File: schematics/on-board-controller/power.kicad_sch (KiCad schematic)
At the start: 20 parts, among them J3 xt60, U6 L78L33_TO92, U7 L7806

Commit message: changed size of electrolytic capacitors
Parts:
- C4, C5, C6: footprint Capacitor_THT:CP_Radial_D14.0mm_P7.50mm -> Capacitor_THT:CP_Radial_D12.5mm_P5.00mm
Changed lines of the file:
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@@
 			)
 		)
-		(property "Footprint" "Capacitor_THT:CP_Radial_D14.0mm_P7.50mm"
+		(property "Footprint" "Capacitor_THT:CP_Radial_D12.5mm_P5.00mm"
 			(at 144.4752 100.33 0)
 			(effects
@@
 			)
 		)
-		(property "Footprint" "Capacitor_THT:CP_Radial_D14.0mm_P7.50mm"
+		(property "Footprint" "Capacitor_THT:CP_Radial_D12.5mm_P5.00mm"
 			(at 67.0052 77.47 0)
 			(effects
@@
 			)
 		)
-		(property "Footprint" "Capacitor_THT:CP_Radial_D14.0mm_P7.50mm"
+		(property "Footprint" "Capacitor_THT:CP_Radial_D12.5mm_P5.00mm"
 			(at 87.63 45.4152 0)
 			(effects

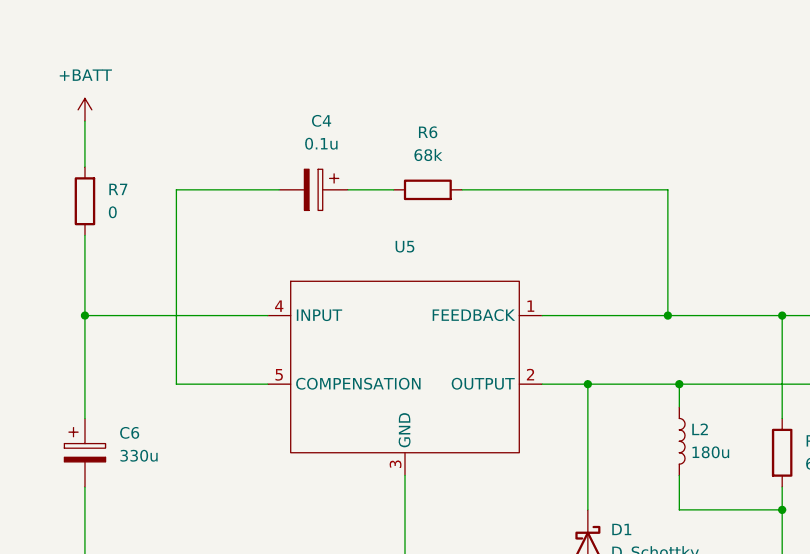
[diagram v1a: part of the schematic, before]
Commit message: updated names of components on schematic
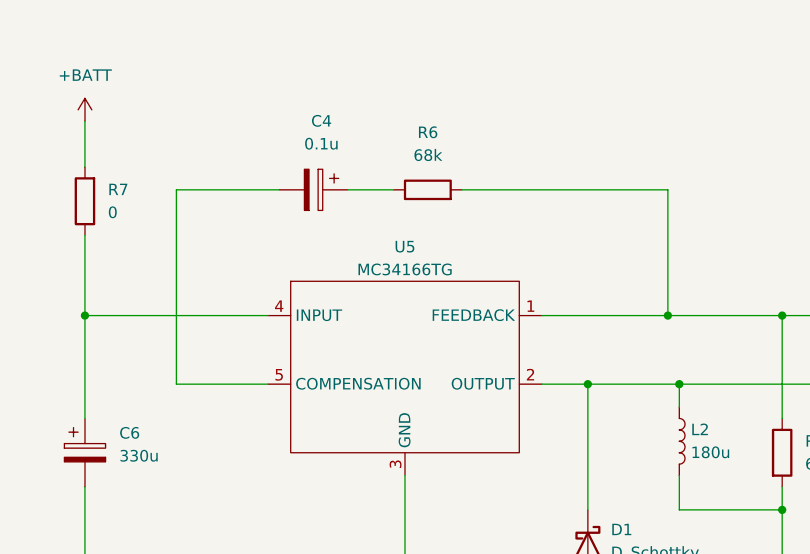
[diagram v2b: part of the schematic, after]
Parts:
- U5: value ~ -> MC34166TG
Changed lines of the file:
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@@
 			)
 		)
-		(property "Value" "~"
+		(property "Value" "MC34166TG"
 			(at 101.6 53.34 0)
 			(effects

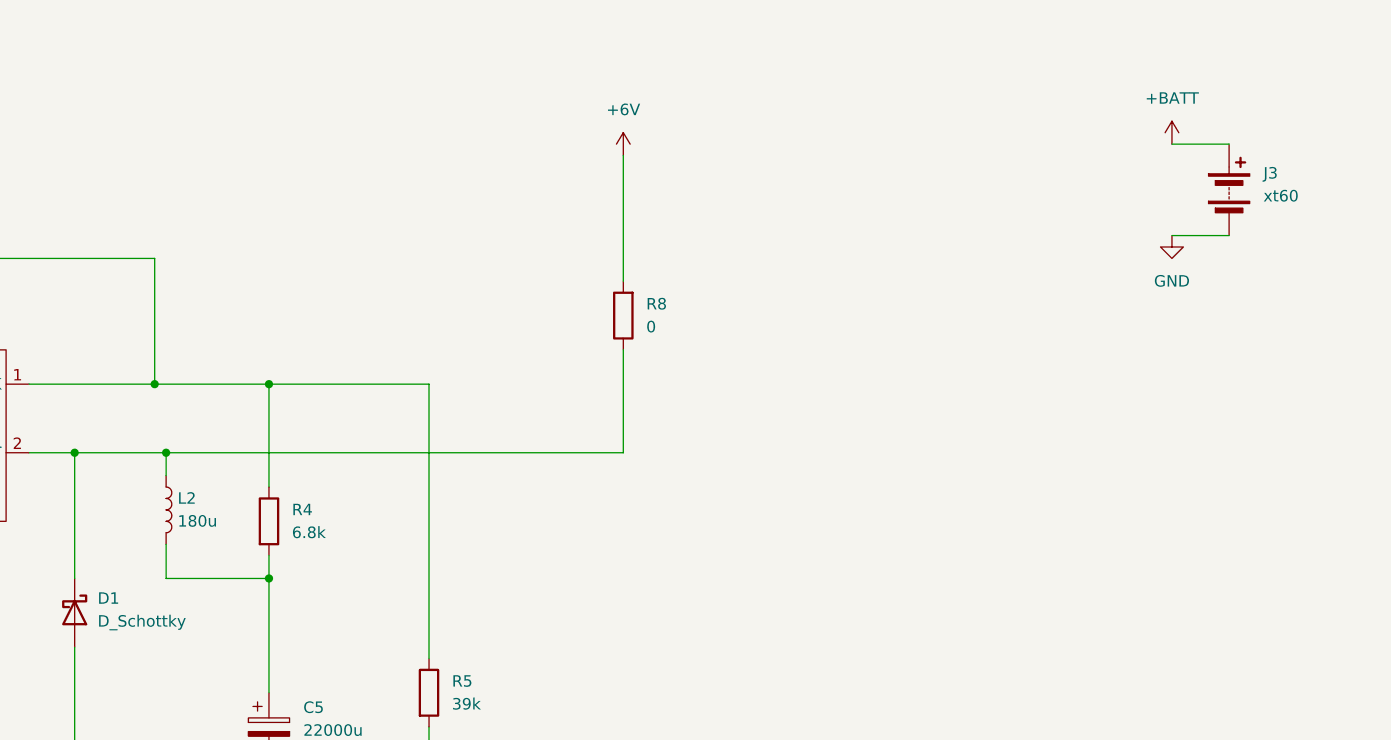
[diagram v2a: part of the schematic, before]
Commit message: updated on-board schematic with changes
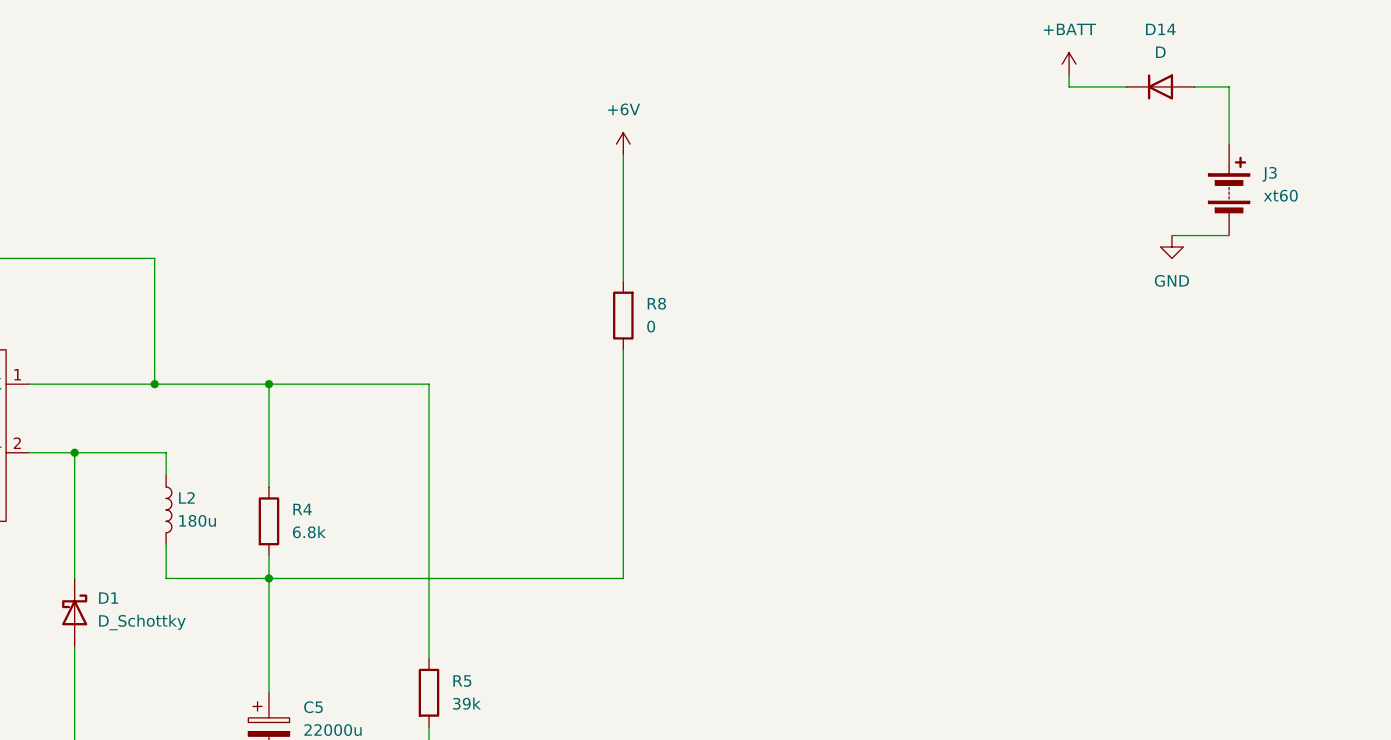
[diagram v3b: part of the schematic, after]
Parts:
- added D14: D, LED_SMD:LED_0805_2012Metric_Pad1.15x1.40mm_HandSolder, symbol Device:D
- C4: footprint Capacitor_THT:CP_Radial_D12.5mm_P5.00mm -> Capacitor_THT:CP_Radial_D5.0mm_P2.50mm
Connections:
- net +BATT: now also D14.1 (K); no longer J3.1 (+)
- net at D1.1 (K), L2.1, U5.2 (OUTPUT): no longer R8.1
- net at C5.1, L2.2, R4.2: now also R8.1
- new net: D14.2 (A), J3.1 (+)
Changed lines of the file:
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@@
-	)
-	(junction
-		(at 132.08 66.04)
-		(diameter 0)
-		(color 0 0 0 0)
 	)
 	(junction
@@
 	(wire
 		(pts
-			(xy 243.84 31.75) (xy 250.19 31.75)
+			(xy 232.41 24.13) (xy 232.41 25.4)
+		)
+		(stroke
+			(width 0)
+			(type default)
+		)
+	)
+	(wire
+		(pts
+			(xy 250.19 25.4) (xy 250.19 31.75)
 		)
 		(stroke
@@
 	(wire
 		(pts
-			(xy 182.88 54.61) (xy 182.88 66.04)
+			(xy 182.88 54.61) (xy 182.88 80.01)
 		)
 		(stroke
@@
 	(wire
 		(pts
+			(xy 232.41 25.4) (xy 238.76 25.4)
+		)
+		(stroke
+			(width 0)
+			(type default)
+		)
+	)
+	(wire
+		(pts
 			(xy 121.92 111.76) (xy 143.51 111.76)
 		)
@@
 	(wire
 		(pts
-			(xy 132.08 66.04) (xy 182.88 66.04)
-		)
-		(stroke
-			(width 0)
-			(type default)
-		)
-	)
-	(wire
-		(pts
 			(xy 66.04 77.47) (xy 66.04 111.76)
 		)
@@
 	(wire
 		(pts
+			(xy 246.38 25.4) (xy 250.19 25.4)
+		)
+		(stroke
+			(width 0)
+			(type default)
+		)
+	)
+	(wire
+		(pts
 			(xy 130.81 58.42) (xy 116.84 58.42)
 		)
@@
 		(pts
 			(xy 143.51 92.71) (xy 143.51 80.01)
+		)
+		(stroke
+			(width 0)
+			(type default)
+		)
+	)
+	(wire
+		(pts
+			(xy 182.88 80.01) (xy 143.51 80.01)
 		)
 		(stroke
@@
 	(symbol
 		(lib_id "power:+BATT")
-		(at 243.84 31.75 0)
+		(at 232.41 24.13 0)
 		(unit 1)
 		(exclude_from_sim no)
@@
 		(fields_autoplaced yes)
 		(property "Reference" "#PWR029"
-			(at 243.84 35.56 0)
+			(at 232.41 27.94 0)
 			(effects
 				(font
@@
 		)
 		(property "Value" "+BATT"
-			(at 243.84 26.67 0)
+			(at 232.41 19.05 0)
 			(effects
 				(font
@@
 		)
 		(property "Footprint" ""
-			(at 243.84 31.75 0)
+			(at 232.41 24.13 0)
 			(effects
 				(font
@@
 		)
 		(property "Datasheet" ""
-			(at 243.84 31.75 0)
+			(at 232.41 24.13 0)
 			(effects
 				(font
@@
 		)
 		(property "Description" "Power symbol creates a global label with name \"+BATT\""
-			(at 243.84 31.75 0)
+			(at 232.41 24.13 0)
 			(effects
 				(font
@@
 	)
 	(symbol
+		(lib_id "Device:D")
+		(at 242.57 25.4 0)
+		(unit 1)
+		(exclude_from_sim no)
+		(in_bom yes)
+		(on_board yes)
+		(dnp no)
+		(fields_autoplaced yes)
+		(property "Reference" "D14"
+			(at 242.57 19.05 0)
+			(effects
+				(font
+					(size 1.27 1.27)
+				)
+			)
+		)
+		(property "Value" "D"
+			(at 242.57 21.59 0)
+			(effects
+				(font
+					(size 1.27 1.27)
+				)
+			)
+		)
+		(property "Footprint" "LED_SMD:LED_0805_2012Metric_Pad1.15x1.40mm_HandSolder"
+			(at 242.57 25.4 0)
+			(effects
+				(font
+					(size 1.27 1.27)
+				)
+				(hide yes)
+			)
+		)
+		(property "Datasheet" "~"
+			(at 242.57 25.4 0)
+			(effects
+				(font
+					(size 1.27 1.27)
+				)
+				(hide yes)
+			)
+		)
+		(property "Description" "Diode"
+			(at 242.57 25.4 0)
+			(effects
+				(font
+					(size 1.27 1.27)
+				)
+				(hide yes)
+			)
+		)
+		(property "Sim.Device" "D"
+			(at 242.57 25.4 0)
+			(effects
+				(font
+					(size 1.27 1.27)
+				)
+				(hide yes)
+			)
+		)
+		(property "Sim.Pins" "1=K 2=A"
+			(at 242.57 25.4 0)
+			(effects
+				(font
+					(size 1.27 1.27)
+				)
+				(hide yes)
+			)
+		)
+		(pin "2"
+		)
+		(pin "1"
+		)
+		(instances
+			(project "sub"
+				(path "/aba2230e-80ca-41f8-a78f-a68ad044f9a5/2700eb3f-a209-43ae-889c-058ebf494c7c"
+					(reference "D14")
+					(unit 1)
+				)
+			)
+		)
+	)
+	(symbol
 		(lib_id "Device:C")
 		(at 232.41 123.19 0)
@@
 			)
 		)
-		(property "Footprint" "Capacitor_THT:CP_Radial_D12.5mm_P5.00mm"
+		(property "Footprint" "Capacitor_THT:CP_Radial_D5.0mm_P2.50mm"
 			(at 87.63 45.4152 0)
 			(effects

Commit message: on-board: updated schematic to match STM32 confighuration
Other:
- title: sumbersible -> On-board Controller
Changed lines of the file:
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@@
 	(paper "A4")
 	(title_block
-		(title "sumbersible")
+		(title "On-board Controller")
 		(date "2024-07-16")
 		(rev "1")
